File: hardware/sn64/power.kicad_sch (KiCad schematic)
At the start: 146 parts, among them Q301 BSS138BK, Q302 BSS138BK, Q303 BSS138BK, Q304 BSS138BK, Q305 BSS138BK, Q306 BSS138BK, Q307 BSS138BK, Q308 BSS138BK, U301 TUSB320IRWBR, U302 TPS259470LRPWR, U303 TPS259470LRPWR, U304 TPS63070RNMR, U305 TLV62569DBVR, U306 TLV62569DBVR, U307 TLV62569DBVR, U308 TPS22918DBVR, U309 TPS259470LRPWR, U310 TPS3700DDCR, U311 TPS3700DDCR, U312 TPS3700DDCR, U313 TPS3700DDCR, U314 TPS3700DDCR, U315 TPS3700DDCR, U316 TPS3808G01DBVR, U317 TMP302ADRLR

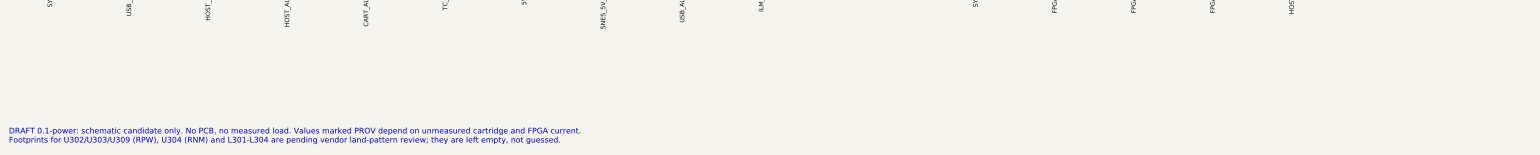
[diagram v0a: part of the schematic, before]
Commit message: Footprints for the eFuses, TPS63070 and inductors from manufacturer land patterns; all 419 parts have footprints
Co-Authored-By: Claude Fable 5.1 <noreply@anthropic.com>
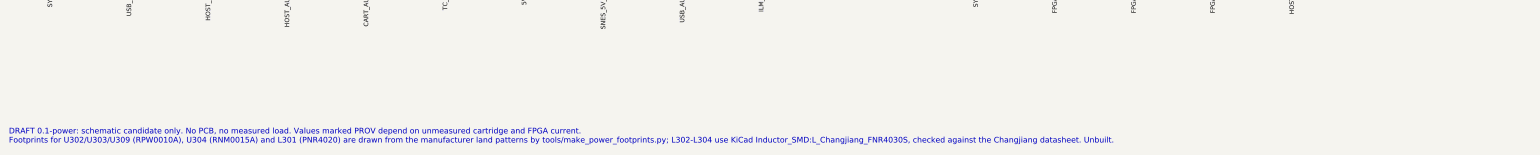
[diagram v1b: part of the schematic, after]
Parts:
- L301: footprint (none) -> SN64:L_APV_PNR4020
- L302, L303, L304: footprint (none) -> Inductor_SMD:L_Changjiang_FNR4030S
- U302, U303, U309: footprint (none) -> SN64:Texas_RPW0010A_VQFN-HR-10_2x2mm; Footprint_status RPW0010A land pattern pending (TI mechanical drawing); not 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 -> RPW0010A from TI 4225183/A example board layout (tools/make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
- U304: footprint (none) -> SN64:Texas_RNM0015A_VQFN-HR-15_2.5x3mm; Footprint_status RNM0015A land pattern pending (TI mechanical drawing); not 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 -> RNM0015A from TI SLVSC58B example board layout (tools/make_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
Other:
- note added: "DRAFT 0.1-power: schematic candidate only. No PCB, no measured load. Values marked PROV depend on unmeasured cartridge and FPGA current. Footprints for U302/U303/U309 (RPW0010A), U304 (RNM0015A) and L301 (PNR4020) are drawn from the manufacturer land patterns by tools/make_power_footprints.py; L302-L304 use KiCad Inductor_SMD:L_Changjiang_FNR4030S, checked against the Changjiang datasheet. Unbuil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"
- note removed: "DRAFT 0.1-power: schematic candidate only. No PCB, no measured load. Values marked PROV depend on unmeasured cartridge and FPGA current. Footprints for U302/U303/U309 (RPW), U304 (RNM) and L301-L304 are pending vendor land-pattern review; they are left empty, not guessed."
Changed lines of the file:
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@@
 (property "Reference" "U302" (at 226.06 55.88 0) (effects (font (size 1.27 1.27)) (justify left)))
 (property "Value" "TPS259470LRPWR" (at 226.06 58.42 0) (effects (font (size 1.27 1.27)) (justify left)))
-(property "Footprint" "" (at 256.54 76.2 0) (effects (font (size 1.27 1.27)) (hide yes)))
+(property "Footprint" "SN64:Texas_RPW0010A_VQFN-HR-10_2x2mm" (at 256.54 76.2 0) (effects (font (size 1.27 1.27)) (hide yes)))
 (property "Datasheet" "https://www.ti.com/lit/ds/symlink/tps25947.pdf" (at 256.54 76.2 0) (effects (font (size 1.27 1.27)) (hide yes)))
 (property "LCSC" "C3662793" (at 256.54 76.2 0) (effects (font (size 1.27 1.27)) (hide yes)))
-(property "Footprint_status" "RPW0010A land pattern pending (TI mechanical drawing); not guessed" (at 256.54 76.2 0) (effects (font (size 1.27 1.27)) (hide yes)))
+(property "Footprint_status" "RPW0010A from TI 4225183/A example board layout (tools/make_power_footprints.py); unbuilt" (at 256.54 76.2 0) (effects (font (size 1.27 1.27)) (hide yes)))
 (pin "1")
 (pin "2")
@@
 (property "Reference" "U303" (at 302.26 55.88 0) (effects (font (size 1.27 1.27)) (justify left)))
 (property "Value" "TPS259470LRPWR" (at 302.26 58.42 0) (effects (font (size 1.27 1.27)) (justify left)))
-(property "Footprint" "" (at 332.74 76.2 0) (effects (font (size 1.27 1.27)) (hide yes)))
+(property "Footprint" "SN64:Texas_RPW0010A_VQFN-HR-10_2x2mm" (at 332.74 76.2 0) (effects (font (size 1.27 1.27)) (hide yes)))
 (property "Datasheet" "https://www.ti.com/lit/ds/symlink/tps25947.pdf" (at 332.74 76.2 0) (effects (font (size 1.27 1.27)) (hide yes)))
 (property "LCSC" "C3662793" (at 332.74 76.2 0) (effects (font (size 1.27 1.27)) (hide yes)))
-(property "Footprint_status" "RPW0010A land pattern pending (TI mechanical drawing); not guessed" (at 332.74 76.2 0) (effects (font (size 1.27 1.27)) (hide yes)))
+(property "Footprint_status" "RPW0010A from TI 4225183/A example board layout (tools/make_power_footprints.py); unbuilt" (at 332.74 76.2 0) (effects (font (size 1.27 1.27)) (hide yes)))
 (pin "1")
 (pin "2")
@@
 (property "Reference" "U309" (at 378.46 55.88 0) (effects (font (size 1.27 1.27)) (justify left)))
 (property "Value" "TPS259470LRPWR" (at 378.46 58.42 0) (effects (font (size 1.27 1.27)) (justify left)))
-(property "Footprint" "" (at 408.94 76.2 0) (effects (font (size 1.27 1.27)) (hide yes)))
+(property "Footprint" "SN64:Texas_RPW0010A_VQFN-HR-10_2x2mm" (at 408.94 76.2 0) (effects (font (size 1.27 1.27)) (hide yes)))
 (property "Datasheet" "https://www.ti.com/lit/ds/symlink/tps25947.pdf" (at 408.94 76.2 0) (effects (font (size 1.27 1.27)) (hide yes)))
 (property "LCSC" "C3662793" (at 408.94 76.2 0) (effects (font (size 1.27 1.27)) (hide yes)))
-(property "Footprint_status" "RPW0010A land pattern pending (TI mechanical drawing); not guessed" (at 408.94 76.2 0) (effects (font (size 1.27 1.27)) (hide yes)))
+(property "Footprint_status" "RPW0010A from TI 4225183/A example board layout (tools/make_power_footprints.py); unbuilt" (at 408.94 76.2 0) (effects (font (size 1.27 1.27)) (hide yes)))
 (pin "1")
 (pin "2")
@@
 (property "Reference" "U304" (at 30.48 149.86 0) (effects (font (size 1.27 1.27)) (justify left)))
 (property "Value" "TPS63070RNMR" (at 30.48 152.4 0) (effects (font (size 1.27 1.27)) (justify left)))
-(property "Footprint" "" (at 60.96 177.8 0) (effects (font (size 1.27 1.27)) (hide yes)))
+(property "Footprint" "SN64:Texas_RNM0015A_VQFN-HR-15_2.5x3mm" (at 60.96 177.8 0) (effects (font (size 1.27 1.27)) (hide yes)))
 (property "Datasheet" "https://www.ti.com/lit/ds/symlink/tps63070.pdf" (at 60.96 177.8 0) (effects (font (size 1.27 1.27)) (hide yes)))
 (property "LCSC" "C109322" (at 60.96 177.8 0) (effects (font (size 1.27 1.27)) (hide yes)))
-(property "Footprint_status" "RNM0015A land pattern pending (TI mechanical drawing); not guessed" (at 60.96 177.8 0) (effects (font (size 1.27 1.27)) (hide yes)))
+(property "Footprint_status" "RNM0015A from TI SLVSC58B example board layout (tools/make_power_footprints.py); unbuilt" (at 60.96 177.8 0) (effects (font (size 1.27 1.27)) (hide yes)))
 (pin "1")
 (pin "2")
@@
 (property "Reference" "L301" (at 193.04 387.35 0) (effects (font (size 1.27 1.27)) (justify left)))
 (property "Value" "1.5uH PNR4020-1R5M" (at 193.04 389.89 0) (effects (font (size 1.27 1.27)) (justify left)))
-(property "Footprint" "" (at 190.5 388.62 0) (effects (font (size 1.27 1.27)) (hide yes)))
+(property "Footprint" "SN64:L_APV_PNR4020" (at 190.5 388.62 0) (effects (font (size 1.27 1.27)) (hide yes)))
 (property "Datasheet" "" (at 190.5 388.62 0) (effects (font (size 1.27 1.27)) (hide yes)))
 (property "MPN" "PNR4020-1R5M" (at 190.5 388.62 0) (effects (font (size 1.27 1.27)) (hide yes)))
@@
 (property "Reference" "L302" (at 406.4 387.35 0) (effects (font (size 1.27 1.27)) (justify left)))
 (property "Value" "2.2uH FNR4030S2R2MT" (at 406.4 389.89 0) (effects (font (size 1.27 1.27)) (justify left)))
-(property "Footprint" "" (at 403.86 388.62 0) (effects (font (size 1.27 1.27)) (hide yes)))
+(property "Footprint" "Inductor_SMD:L_Changjiang_FNR4030S" (at 403.86 388.62 0) (effects (font (size 1.27 1.27)) (hide yes)))
 (property "Datasheet" "" (at 403.86 388.62 0) (effects (font (size 1.27 1.27)) (hide yes)))
 (property "MPN" "FNR4030S2R2MT" (at 403.86 388.62 0) (effects (font (size 1.27 1.27)) (hide yes)))
@@
 (property "Reference" "L303" (at 530.86 387.35 0) (effects (font (size 1.27 1.27)) (justify left)))
 (property "Value" "2.2uH FNR4030S2R2MT" (at 530.86 389.89 0) (effects (font (size 1.27 1.27)) (justify left)))
-(property "Footprint" "" (at 528.32 388.62 0) (effects (font (size 1.27 1.27)) (hide yes)))
+(property "Footprint" "Inductor_SMD:L_Changjiang_FNR4030S" (at 528.32 388.62 0) (effects (font (size 1.27 1.27)) (hide yes)))
 (property "Datasheet" "" (at 528.32 388.62 0) (effects (font (size 1.27 1.27)) (hide yes)))
 (property "MPN" "FNR4030S2R2MT" (at 528.32 388.62 0) (effects (font (size 1.27 1.27)) (hide yes)))
@@
 (property "Reference" "L304" (at 121.92 417.83 0) (effects (font (size 1.27 1.27)) (justify left)))
 (property "Value" "2.2uH FNR4030S2R2MT" (at 121.92 420.37 0) (effects (font (size 1.27 1.27)) (justify left)))
-(property "Footprint" "" (at 119.38 419.1 0) (effects (font (size 1.27 1.27)) (hide yes)))
+(property "Footprint" "Inductor_SMD:L_Changjiang_FNR4030S" (at 119.38 419.1 0) (effects (font (size 1.27 1.27)) (hide yes)))
 (property "Datasheet" "" (at 119.38 419.1 0) (effects (font (size 1.27 1.27)) (hide yes)))
 (property "MPN" "FNR4030S2R2MT" (at 119.38 419.1 0) (effects (font (size 1.27 1.27)) (hide yes)))
@@
 (text "CARTRIDGE 5 V: U309 TPS259470L, EN/UVLO default low (Q306 clamp until cart_5v_enable), UVLO 4.64 V / OVLO 5.48 V rising,\nILIM 1.00 A (PROV), dVdt 680 pF (PROV), ITIMER 1.2 nF. Q307 + R328 470R discharge while inhibited (<=12 mA into an energized rail).\nINTERFACE_3V3: U308 TPS22918, ON default low (R340 1k), CT 470 pF, QOD via R341 100R." (at 20.32 152.4 0) (effects (font (size 1.27 1.27)) (justify left top)))
 (text "MONITORS (all powered from FPGA_3V3, outputs pulled up to FPGA_3V3 = 3.3 V-safe; supply loss reads NOT OK):\nU310 SYS_VIN -> host_3v3_ok | U311-U313 FPGA rails -> fpga_rails_ok | U314 SNES_5V_CART (socket side) -> cart_5v_ok |\nU315 INTERFACE_3V3 -> iface_rail_ok | U309 FLT (10k to FPGA_3V3) -> efuse_fault_n | U317 TMP302A + Q308 -> overtemp (1 = hot or sensor dead)." (at 20.32 241.3 0) (effects (font (size 1.27 1.27)) (justify left top)))
-(text "DRAFT 0.1-power: schematic candidate only. No PCB, no measured load. Values marked PROV depend on unmeasured cartridge and FPGA current.\nFootprints for U302/U303/U309 (RPW), U304 (RNM) and L301-L304 are pending vendor land-pattern review; they are left empty, not guessed." (at 20.32 518.16 0) (effects (font (size 1.27 1.27)) (justify left top)))
+(text "DRAFT 0.1-power: schematic candidate only. No PCB, no measured load. Values marked PROV depend on unmeasured cartridge and FPGA current.\nFootprints for U302/U303/U309 (RPW0010A), U304 (RNM0015A) and L301 (PNR4020) are drawn from the manufacturer land patterns by tools/make_power_footprints.py; L302-L304 use KiCad Inductor_SMD:L_Changjiang_FNR4030S, checked against the Changjiang datasheet. Unbuilt." (at 20.32 518.16 0) (effects (font (size 1.27 1.27)) (justify left top)))
 (sheet_instances (path "/e2505a21-9627-547b-aef4-ab0d2c57bd10/4c37b7d7-17a3-5df8-bbfc-6c34ee2cc3b6" (page "4"))) (embedded_fonts no))
